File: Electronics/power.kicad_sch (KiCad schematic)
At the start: 42 parts, among them J4 Battery 1S2P, SW3 SW_SPST, U10 AP9101CK, U11 AP2112K-3.3, U12 INA138, U8 TP4056, U9 FP6298

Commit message: made some changes
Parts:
- added C28: 10uF, Capacitor_SMD:C_0805_2012Metric_Pad1.18x1.45mm_HandSolder, symbol Device:C_Small
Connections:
- net GND: now also C28.2
- net PowerInInrush: now also C28.1
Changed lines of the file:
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@@
   (junction (at 80.01 48.26) (diameter 0) (color 0 0 0 0))
   (junction (at 80.01 52.07) (diameter 0) (color 0 0 0 0))
+  (junction (at 80.01 54.61) (diameter 0) (color 0 0 0 0))
   (junction (at 86.36 100.33) (diameter 0) (color 0 0 0 0))
   (junction (at 97.79 44.45) (diameter 0) (color 0 0 0 0))
@@
     (stroke (width 0) (type default) (color 0 0 0 0))
   )
+  (wire (pts (xy 80.01 54.61) (xy 80.01 58.42))
+    (stroke (width 0) (type default) (color 0 0 0 0))
+  )
+  (wire (pts (xy 80.01 63.5) (xy 80.01 72.39))
+    (stroke (width 0) (type default) (color 0 0 0 0))
+  )
   (wire (pts (xy 83.82 52.07) (xy 80.01 52.07))
     (stroke (width 0) (type default) (color 0 0 0 0))
@@
     )
     (property "Datasheet" "" (id 3) (at 76.2 113.03 0)
+      (effects (font (size 1.27 1.27)) hide)
+    )
+    (pin "1")
+  )
+  (symbol (lib_id "power:GND") (at 80.01 72.39 0) (unit 1)
+    (in_bom yes) (on_board yes)
+    (property "Reference" "#PWR0102" (id 0) (at 80.01 78.74 0)
+      (effects (font (size 1.27 1.27)) hide)
+    )
+    (property "Value" "GND" (id 1) (at 80.137 76.7842 0))
+    (property "Footprint" "" (id 2) (at 80.01 72.39 0)
+      (effects (font (size 1.27 1.27)) hide)
+    )
+    (property "Datasheet" "" (id 3) (at 80.01 72.39 0)
       (effects (font (size 1.27 1.27)) hide)
     )
@@
       (effects (font (size 1.27 1.27)) hide)
     )
+    (pin "1")
+    (pin "2")
+  )
+  (symbol (lib_id "Device:C_Small") (at 80.01 60.96 0) (unit 1)
+    (in_bom yes) (on_board yes) (fields_autoplaced)
+    (property "Reference" "C28" (id 0) (at 77.47 59.6899 0)
+      (effects (font (size 1.27 1.27)) (justify right))
+    )
+    (property "Value" "10uF" (id 1) (at 77.47 62.2299 0)
+      (effects (font (size 1.27 1.27)) (justify right))
+    )
+    (property "Footprint" "Capacitor_SMD:C_0805_2012Metric_Pad1.18x1.45mm_HandSolder" (id 2) (at 80.9752 64.77 0)
+      (effects (font (size 1.27 1.27)) hide)
+    )
+    (property "Datasheet" "~" (id 3) (at 80.01 60.96 0)
+      (effects (font (size 1.27 1.27)) hide)
+    )

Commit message: del backups
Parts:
- renumbered C13 to C14, C14 to C15, C15 to C16, C28 to C17, C16 to C18, C17 to C19, C18 to C20, C19 to C21, C20 to C22, C21 to C23, C22 to C24, C23 to C25, C24 to C26, J4 to J5, R20 to R24, R21 to R25, R22 to R26, R23 to R27, R24 to R28, R25 to R29, R26 to R30, R27 to R31, R28 to R32, R29 to R33, R30 to R34, R31 to R35, R32 to R36, R33 to R37, R34 to R38, U8 to U10, U9 to U11, U10 to U12, U11 to U13, U12 to U14

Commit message: yep
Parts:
- added C25: 100nF, Capacitor_SMD:C_0805_2012Metric_Pad1.18x1.45mm_HandSolder, symbol Device:C_Small
- U12: renamed from U14; Field4 CHECK!!!! -> (none)
- renumbered C17 to C16, C16 to C17, C26 to C23, C23 to C24, C24 to C26, C25 to C27, R37 to R35, R38 to R36, R35 to R37, R36 to R38, U12 to U14
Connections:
- net +BATT: now also U12.4 (-); no longer R38.2, U12.3 (+)
- net Bat+VE: now also R38.2, U12.3 (+); no longer U12.4 (-)
- net GND: now also C25.2
- net at R38.1, U14.2 (VDD): now also C25.1
- net at U14.3 (VSS): now also J5.3 (Pin_3), J5.4 (Pin_4)
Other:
- moved on the sheet: C17, C18, C21, C22, C23, C24, C26, C27, D1, D3, D6, D7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

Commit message: some changes were made
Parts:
- added U15: FDC6303N, Package_TO_SOT_SMD:SOT-23-6_Handsoldering, symbol FDC6303N:FDC6303N
- renumbered C15 to C14, C16 to C15, C17 to C16, C18 to C17, C19 to C18, C20 to C19, C14 to C20, D3 to D10, D6 to D11, D7 to D12, D2 to D6, D1 to D7, D4 to D8, D5 to D9, R27 to R37, R28 to R38, R29 to R39, R30 to R40, R26 to R41, R32 to R42, R31 to R43, R24 to R44, R25 to R45, R33 to R46, R34 to R47, R35 to R48, R36 to R49, R37 to R50, R38 to R51
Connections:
- net PowerIn is gone; now on net Power In: D12.2 (A)
- net GND: now also U15.4 (D2), U15.5 (S1), U15.6 (D1)
- net bat-ve: now reaches J5.3 (Pin_3), J5.4 (Pin_4), U14.3 (VSS)
- net bat-ve: now also U15.2 (S2)
- net at U14.4 (DO): now also U15.3 (G2)
- net at U14.5 (CO): now also U15.1 (G1)
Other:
- company: Philip McGaw -> Squashed Fly
- moved on the sheet: C14, C15, C18, C19, C20, C23, C25, D6, D8, D9, J5, R37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

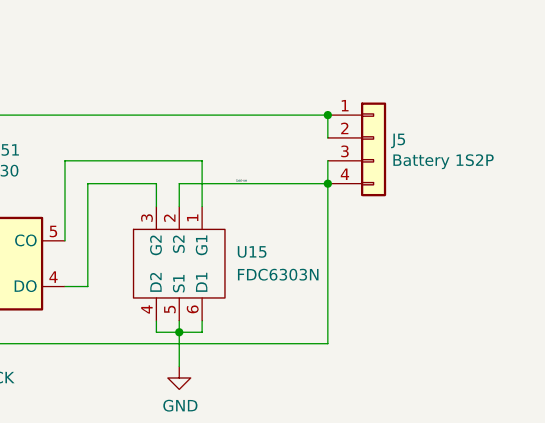
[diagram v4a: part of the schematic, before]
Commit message: removed the backups
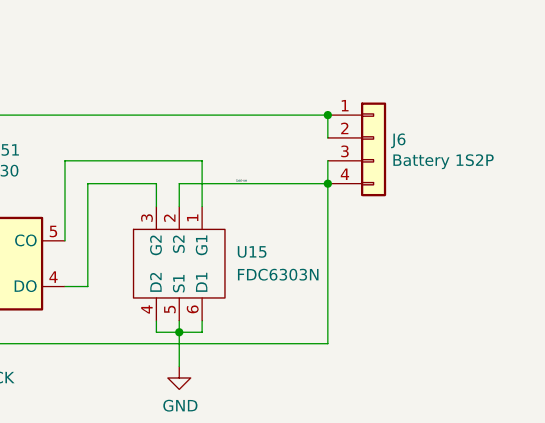
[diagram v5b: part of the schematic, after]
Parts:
- renumbered J5 to J6
